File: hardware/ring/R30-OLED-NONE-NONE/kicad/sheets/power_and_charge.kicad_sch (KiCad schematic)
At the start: 19 parts, among them Q1 SI2301 P-FET, Q2 2N7002 gate driver, U3 TP4054, U4 RT9080-33GJ5

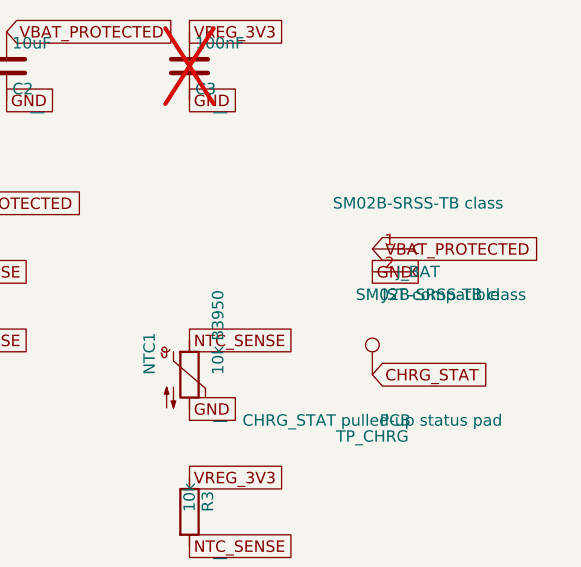
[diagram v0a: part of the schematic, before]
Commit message: fix(r30): model battery connector shield pads
Sensing mechanism: PAW3204 optical surface tracking.

Form factor and angle: R30 30-degree ring, OLED/NONE/NONE active lane.

Intended use: accessibility-first BLE HID pointing first-board validation.

BOM estimate: active R30 prototype remains about $5.30-$9.45, target about $9.
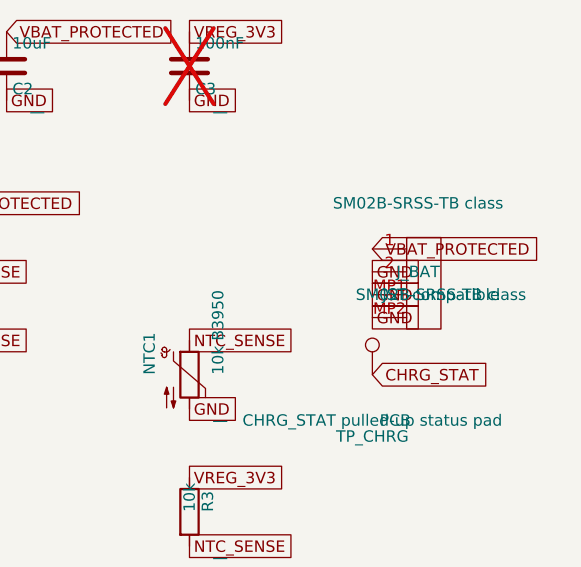
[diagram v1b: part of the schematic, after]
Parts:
- J_BAT: symbol Connector:Conn_01x02_Socket -> PowerFinger:JST_SH_SM02B_SRSS_TB_RA_FirstBoard
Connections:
- net GND: now also J_BAT.MP1 (SHIELD), J_BAT.MP2 (SHIELD)
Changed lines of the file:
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@@
 	)
 	(symbol
-		(lib_id "Connector:Conn_01x02_Socket")
+		(lib_id "PowerFinger:JST_SH_SM02B_SRSS_TB_RA_FirstBoard")
 		(at 195.58 130.81 0)
 		(unit 1)
@@
 		)
 		(pin "2"
+		)
+		(pin "MP1"
+		)
+		(pin "MP2"
 		)
 		(instances
@@
 		(effects
 			(font
+				(size 1.27 1.27)
+			)
+			(justify left bottom)
+		)
+	)
+	(global_label "GND"
+		(shape passive)
+		(at 190.5 135.89 0)
+		(effects
+			(font
+				(size 1.27 1.27)
+			)
+			(justify left bottom)
+		)
+	)
+	(global_label "GND"
+		(shape passive)
+		(at 190.5 138.43 0)
+		(effects
+			(font

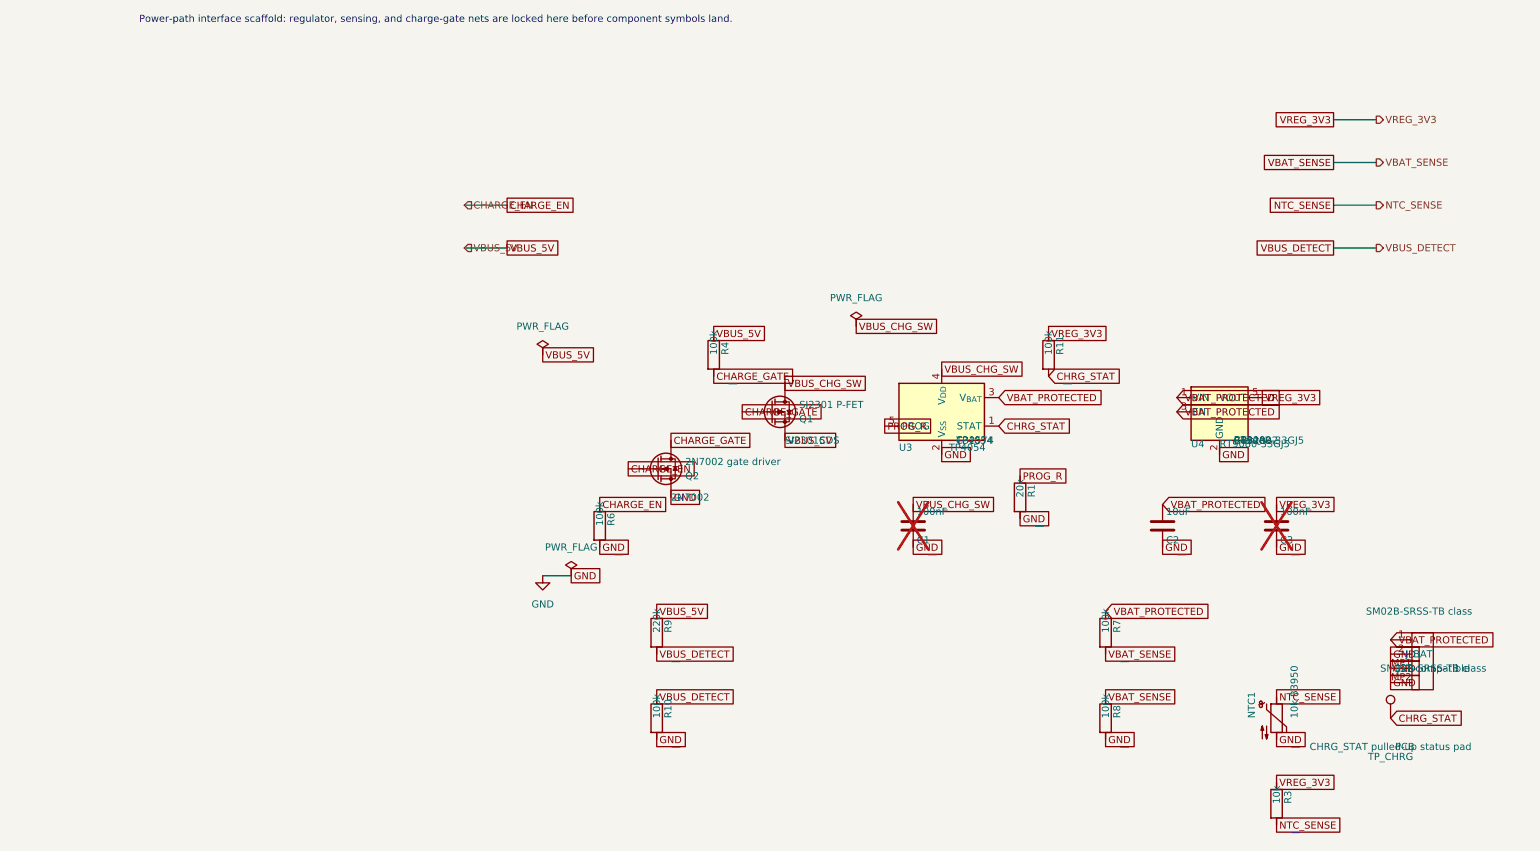
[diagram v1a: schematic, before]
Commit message: feat(r30): cut service hardware blockers
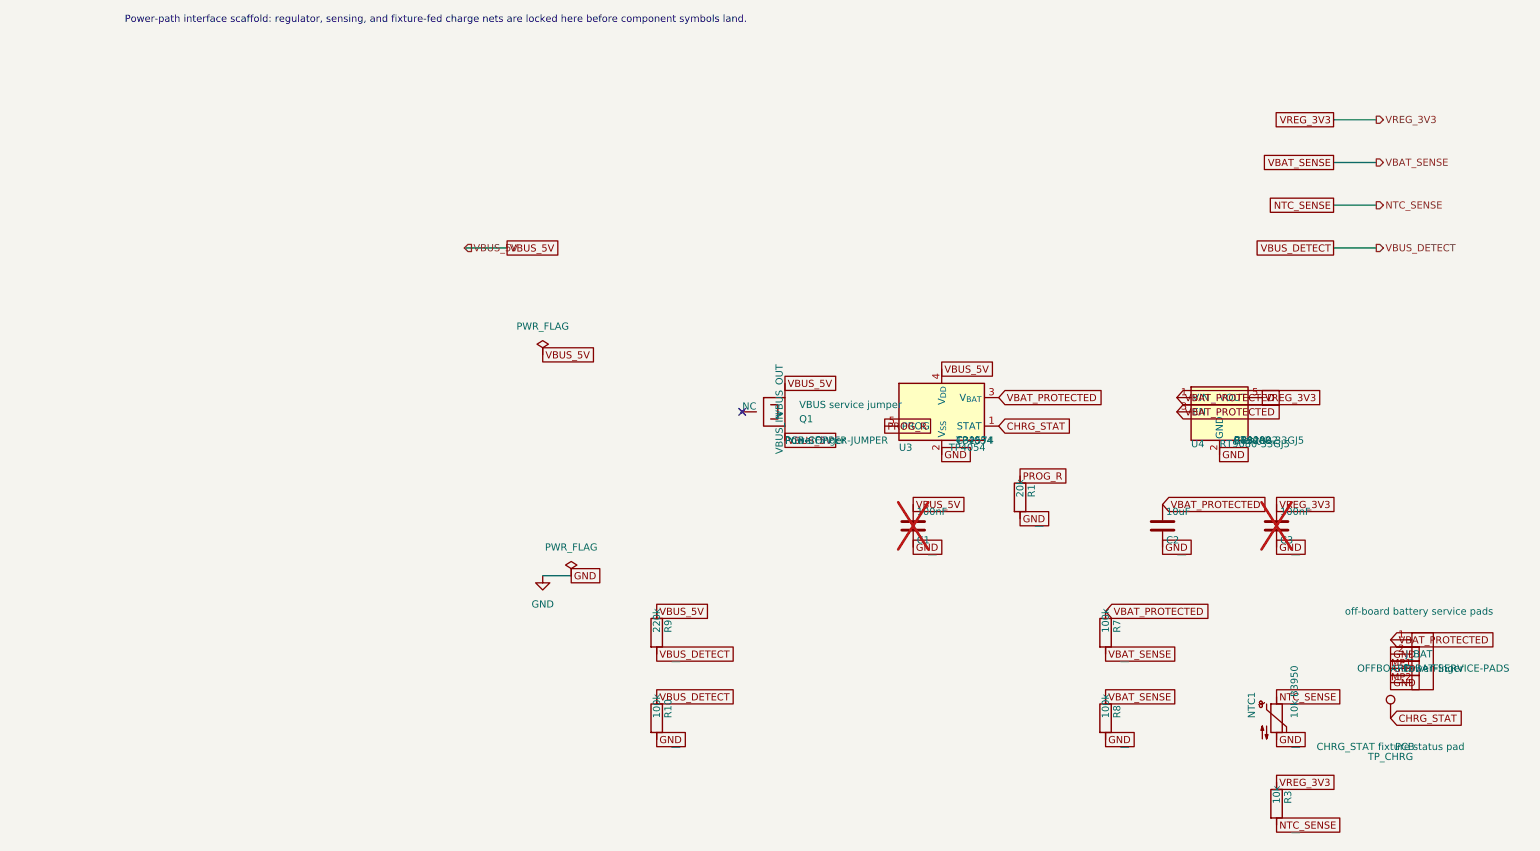
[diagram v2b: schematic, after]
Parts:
- removed Q2: 2N7002 gate driver, Package_TO_SOT_SMD:SOT-23, symbol PowerFinger:2N7002_SOT23_FirstBoard
- removed R11, R4, R6: 100k, Resistor_SMD:R_0402_1005Metric, symbol Device:R
- J_BAT: value SM02B-SRSS-TB class -> off-board battery service pads; footprint PowerFinger_Ring:JST_SH_SM02B-SRSS-TB_RA_1x02_P1.00mm -> PowerFinger_Ring:Offboard_Battery_Service_SameNet; manufacturer JST-compatible -> PowerFinger; mfg_part_num SM02B-SRSS-TB class -> OFFBOARD-BAT-SERVICE-PADS
- Q1: value SI2301 P-FET -> VBUS service jumper; footprint Package_TO_SOT_SMD:SOT-23 -> PowerFinger_Ring:VBUS_Service_Jumper_SOT23Land; symbol PowerFinger:SI2301_SOT23_FirstBoard -> PowerFinger:VBUS_Service_Jumper_SOT23Land; manufacturer — -> PowerFinger; mfg_part_num SI2301CDS -> PCB-COPPER-JUMPER; now left out of the parts list
- TP_CHRG: value CHRG_STAT pulled-up status pad -> CHRG_STAT fixture status pad; footprint TestPoint:TestPoint_Pad_D1.0mm -> PowerFinger_Ring:TestPoint_Pad_D1.0mm_FirstBoard; now left out of the parts list
- U4: footprint Package_TO_SOT_SMD:SOT-23-5 -> PowerFinger_Ring:RT9080_33GJ5_SOT23_5_ServiceClearance
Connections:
- net VBUS_CHG_SW is gone; now on net VBUS_5V: C1.1, Q1.2 (VBUS_OUT), U3.4 (V_{DD})
- net CHARGE_GATE: no longer names the net of Q1.1 (NC)
- no-connect marks 0 -> 1
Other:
- note added: "Power-path interface scaffold: regulator, sensing, and fixture-fed charge nets are locked here before component symbols land."
- note removed: "Power-path interface scaffold: regulator, sensing, and charge-gate nets are locked here before component symbols land."
